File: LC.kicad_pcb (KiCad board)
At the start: 2 copper layers, 60 x 65 mm, 89 parts, among them J1 INPUT+, J10 DISPLAY, J11 ENTER_BUTTON, J12 UP_BUTTON, J2 INPUT-, J3 Barrel_Jack, J4 EXT_CLK, J5 CLKSRC, J6 SIGSRC, J7 EXT_SIG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

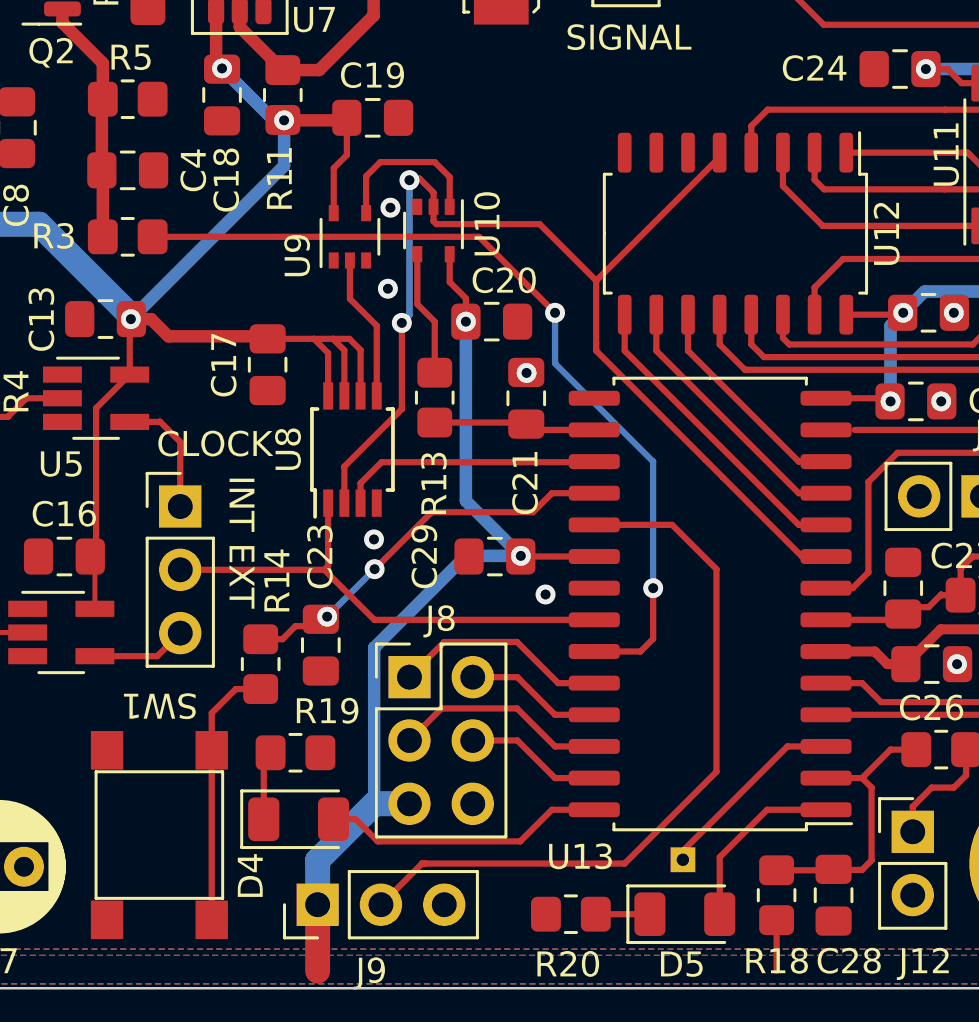
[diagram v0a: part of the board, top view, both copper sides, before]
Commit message: a few more pin swaps
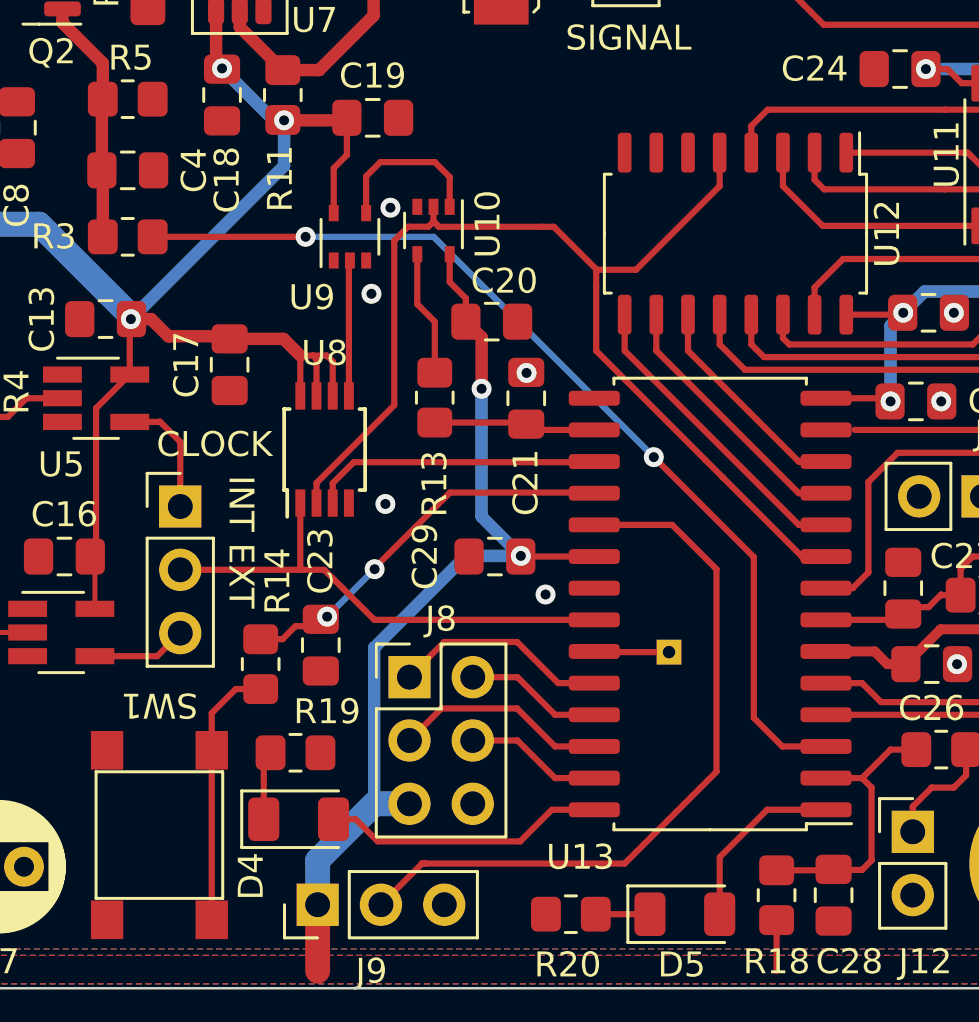
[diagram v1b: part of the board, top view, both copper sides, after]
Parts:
- moved TP1 8.35 mm to (174.8, 86.5)
- moved C17 1.52 mm to (157.1, 75.0)
- moved U8 1.12 mm to (160.9, 78.4)
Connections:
- U13 pad 23: /CAL -> /UNUSED_5
- U13 pad 3: /UNUSED_5 -> /CAL
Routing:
- net /UNUSED_5: track 7.83 -> 3.01 mm
- net /CAL: track 34.7 -> 39.3 mm
- net +5V: track 214.2 -> 211.1 mm
- net /SIG_RED: track 46.6 -> 45.2 mm, vias 2 -> 0
- net /ICP1: track 10.5 -> 11.7 mm
